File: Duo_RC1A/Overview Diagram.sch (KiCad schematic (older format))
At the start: 0 parts

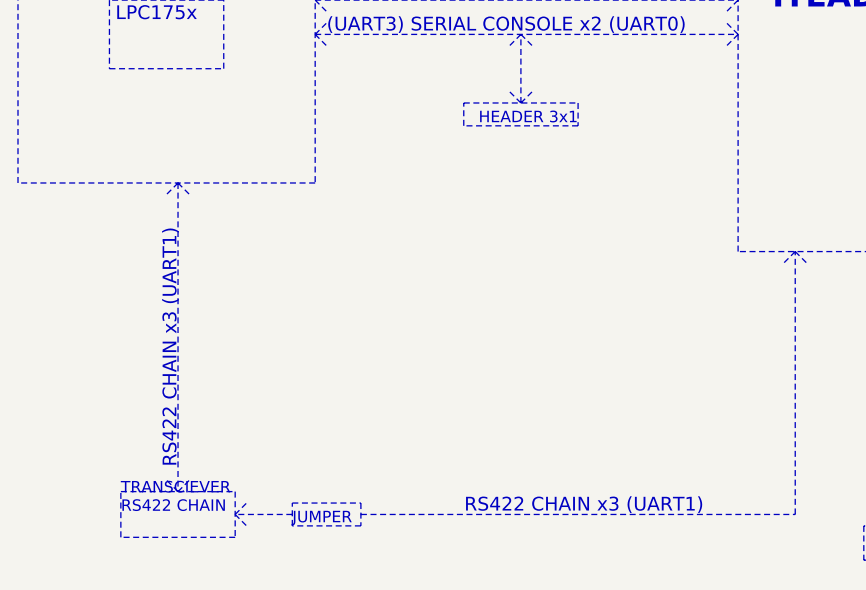
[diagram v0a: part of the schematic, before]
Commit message: wip issue #6: implement full-duplex for the control-chain interface
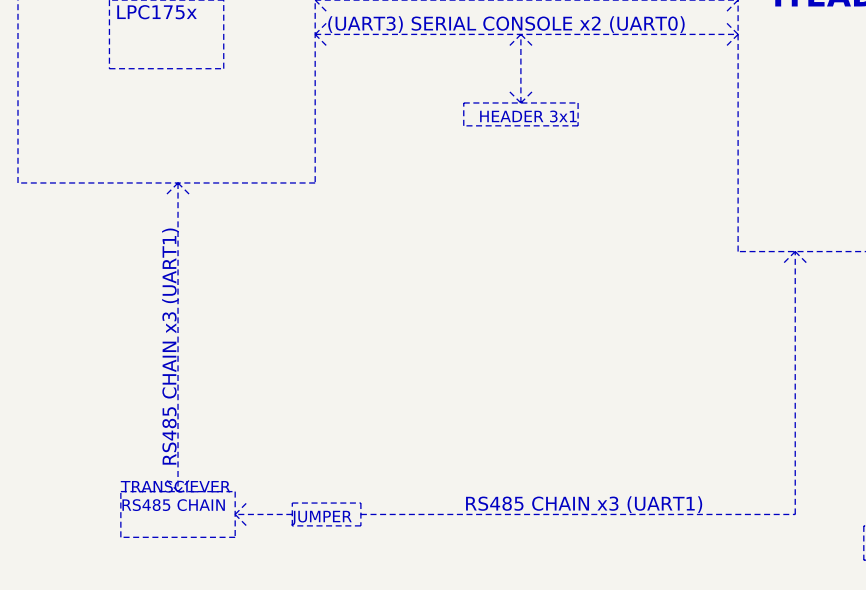
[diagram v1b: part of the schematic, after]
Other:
- note added: "RS485 CHAIN x3 (UART1)"
- note added: "TRANSCIEVER\nRS485 CHAIN"
- note removed: "RS422 CHAIN x3 (UART1)"
- note removed: "TRANSCIEVER\nRS422 CHAIN"
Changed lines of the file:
@@
 HEADER 3x1
 Text Notes 2800 5250 1    60   ~ 0
-RS422 CHAIN x3 (UART1)
+RS485 CHAIN x3 (UART1)
 Wire Notes Line
 	5250 2200 7300 2200
@@
 HMI
 Text Notes 2550 5450 0    50   ~ 0
-TRANSCIEVER\nRS422 CHAIN
+TRANSCIEVER\nRS485 CHAIN
 Wire Notes Line
 	2550 5350 3050 5350
@@
 AUDIO
 Text Notes 5100 5450 2    60   ~ 0
-RS422 CHAIN x3 (UART1)
+RS485 CHAIN x3 (UART1)
 Wire Notes Line
 	5500 4300 5450 4350
